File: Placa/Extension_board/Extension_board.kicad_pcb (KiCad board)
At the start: 2 copper layers, 47 x 29.2 mm, 10 parts, among them J1 USB_B_Micro, J2 USB_B_Micro, J3 Conn_01x06_Male, SW1 SW_PUSHBUTTON, U1 STEVAL-STLCS01V1

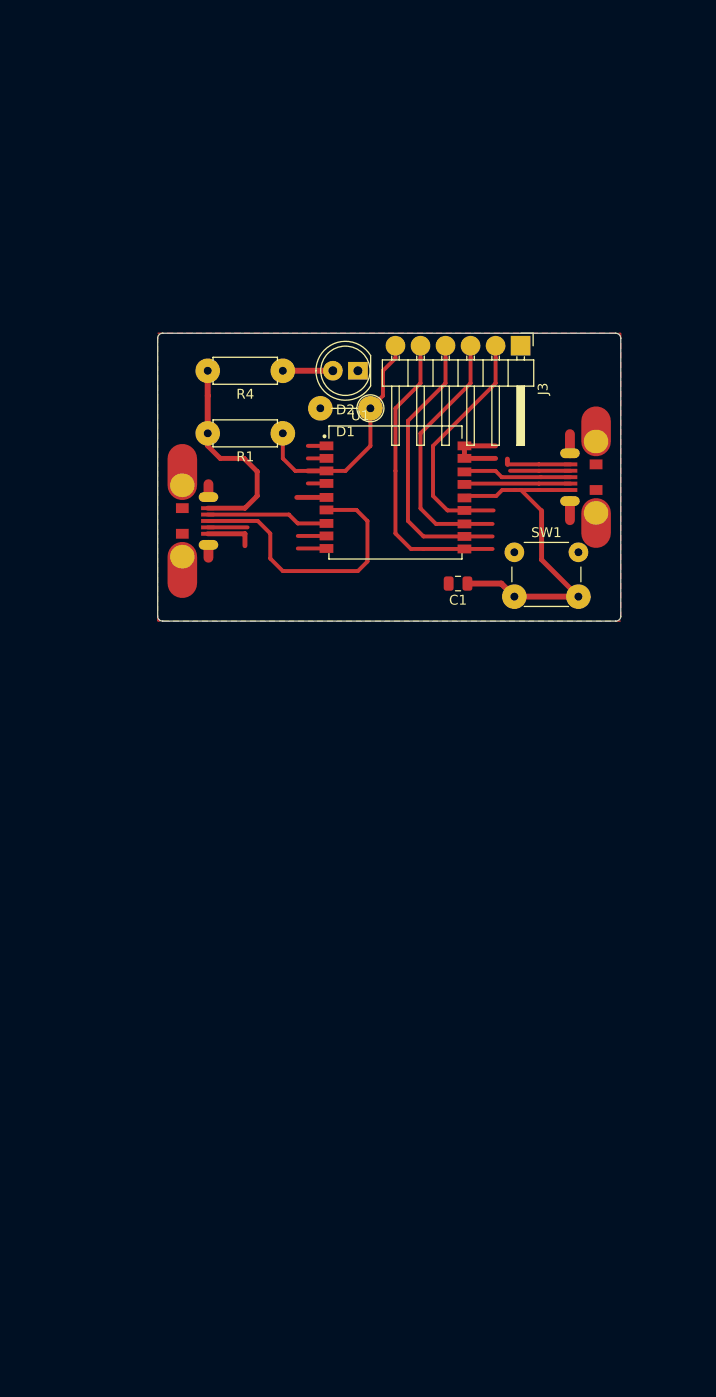
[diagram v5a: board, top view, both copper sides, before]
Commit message: Creacion de app en Qt
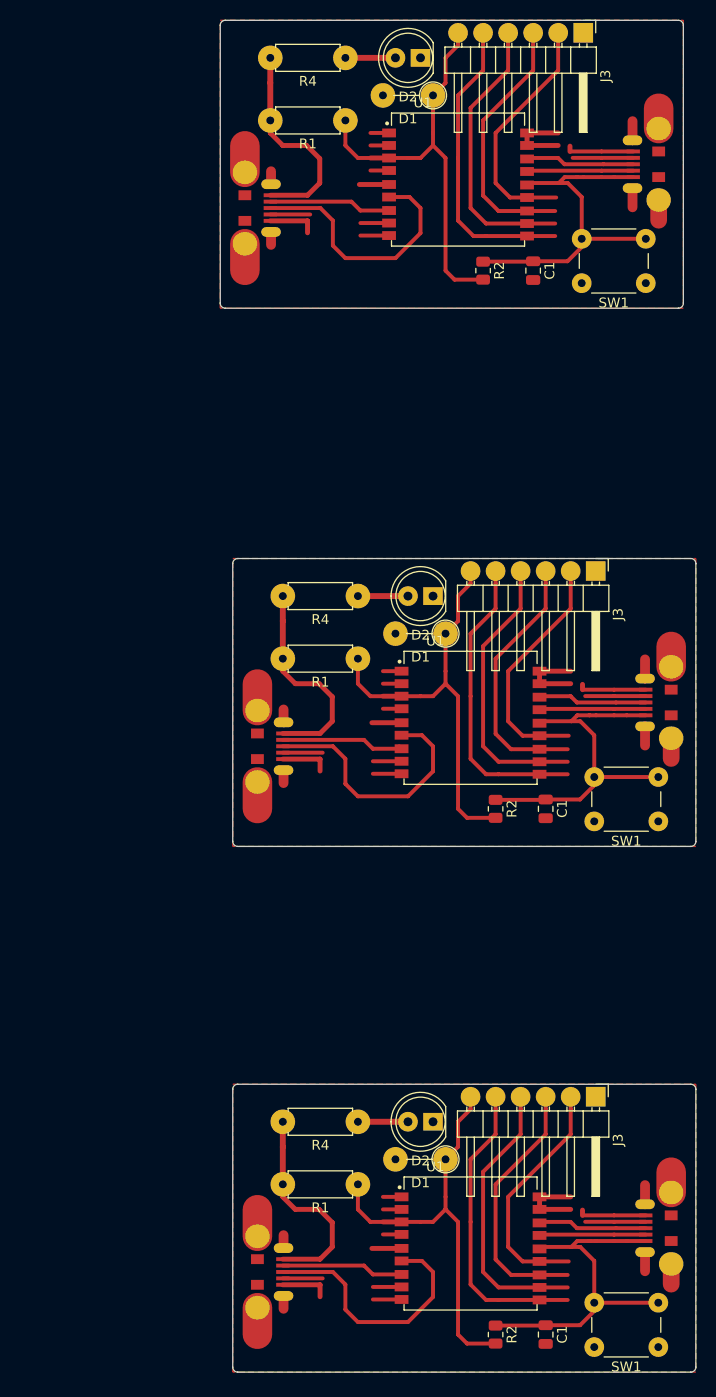
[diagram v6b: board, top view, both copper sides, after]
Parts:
- removed the C1 at (141.0, 86.4)
- added C1: C, Capacitor_SMD:C_0805_2012Metric, F.Cu at (149.9, 162.6)
- added C1: C, Capacitor_SMD:C_0805_2012Metric, F.Cu at (149.9, 109.2)
- added C1: C, Capacitor_SMD:C_0805_2012Metric, F.Cu at (148.6, 54.6)
- added D1: D_Zener, Resistor_THT:R_Axial_DIN0207_L6.3mm_D2.5mm_P5.08mm_Vertical, F.Cu at (139.7, 144.8)
- added D1: D_Zener, Resistor_THT:R_Axial_DIN0207_L6.3mm_D2.5mm_P5.08mm_Vertical, F.Cu at (139.7, 91.4)
- added D2: LED, LED_THT:LED_D5.0mm_IRBlack, F.Cu at (138.4, 141.0)
- added D2: LED, LED_THT:LED_D5.0mm_IRBlack, F.Cu at (138.4, 87.6)
- added J1: USB_B_Micro, freetronics_footprints:USB-MICRO-5pin_PTHMOUNT, F.Cu at (160.0, 151.8)
- added J1: USB_B_Micro, freetronics_footprints:USB-MICRO-5pin_PTHMOUNT, F.Cu at (160.0, 98.4)
- added J2: USB_B_Micro, freetronics_footprints:USB-MICRO-5pin_PTHMOUNT, F.Cu at (123.2, 156.2)
- added J2: USB_B_Micro, freetronics_footprints:USB-MICRO-5pin_PTHMOUNT, F.Cu at (123.2, 102.9)
- added J3: Conn_01x06_Male, Connector_PinHeader_2.54mm:PinHeader_1x06_P2.54mm_Horizontal, F.Cu at (154.9, 138.4)
- added J3: Conn_01x06_Male, Connector_PinHeader_2.54mm:PinHeader_1x06_P2.54mm_Horizontal, F.Cu at (154.9, 85.1)
- added R1: 12Ω, Resistor_THT:R_Axial_DIN0207_L6.3mm_D2.5mm_P7.62mm_Horizontal, F.Cu at (130.8, 147.3)
- added R1: 12Ω, Resistor_THT:R_Axial_DIN0207_L6.3mm_D2.5mm_P7.62mm_Horizontal, F.Cu at (130.8, 94.0)
- added R2: R, Resistor_SMD:R_0805_2012Metric, F.Cu at (144.8, 162.6)
- added R2: R, Resistor_SMD:R_0805_2012Metric, F.Cu at (144.8, 109.2)
- added R2: R, Resistor_SMD:R_0805_2012Metric, F.Cu at (143.5, 54.6)
- added R4: 1kΩ, Resistor_THT:R_Axial_DIN0207_L6.3mm_D2.5mm_P7.62mm_Horizontal, F.Cu at (130.8, 141.0)
- added R4: 1kΩ, Resistor_THT:R_Axial_DIN0207_L6.3mm_D2.5mm_P7.62mm_Horizontal, F.Cu at (130.8, 87.6)
- added SW1: SW_PUSHBUTTON, Button_Switch_THT:SW_PUSH_6mm_H5mm, F.Cu at (161.3, 163.8)
- added SW1: SW_PUSHBUTTON, Button_Switch_THT:SW_PUSH_6mm_H5mm, F.Cu at (161.3, 110.5)
- added U1: STEVAL-STLCS01V1, STEVAL-STLCS01V1_footprint:XDCR_STEVAL-STLCS01V1, F.Cu at (142.2, 153.7)
- added U1: STEVAL-STLCS01V1, STEVAL-STLCS01V1_footprint:XDCR_STEVAL-STLCS01V1, F.Cu at (142.2, 100.3)
- moved J2 32.4 mm to (121.9, 48.3)
- moved D1 32.4 mm to (138.4, 36.8)
- moved J3 32.4 mm to (153.7, 30.5)
- moved R1 32.4 mm to (129.5, 39.4)
- moved U1 32.4 mm to (141.0, 45.7)
- moved D2 32.4 mm to (137.2, 33.0)
- moved J1 32.4 mm to (158.8, 43.8)
- moved R4 32.4 mm to (129.5, 33.0)
- moved SW1 30.4 mm to (160.0, 55.9), turned to 180 degrees
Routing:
- net (no net): track 16.9 -> 692.1 mm
- net /VIN: track 24.2 -> 42.4 mm
- net /RXD-USB_DP: track 28.9 -> 26.1 mm
- added copper zone on F.Cu, net (none)
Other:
- board size 47 x 29.2 mm -> 48.3 x 137.2 mm
